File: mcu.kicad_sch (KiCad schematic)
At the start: 6 parts, among them U3 PCA9358

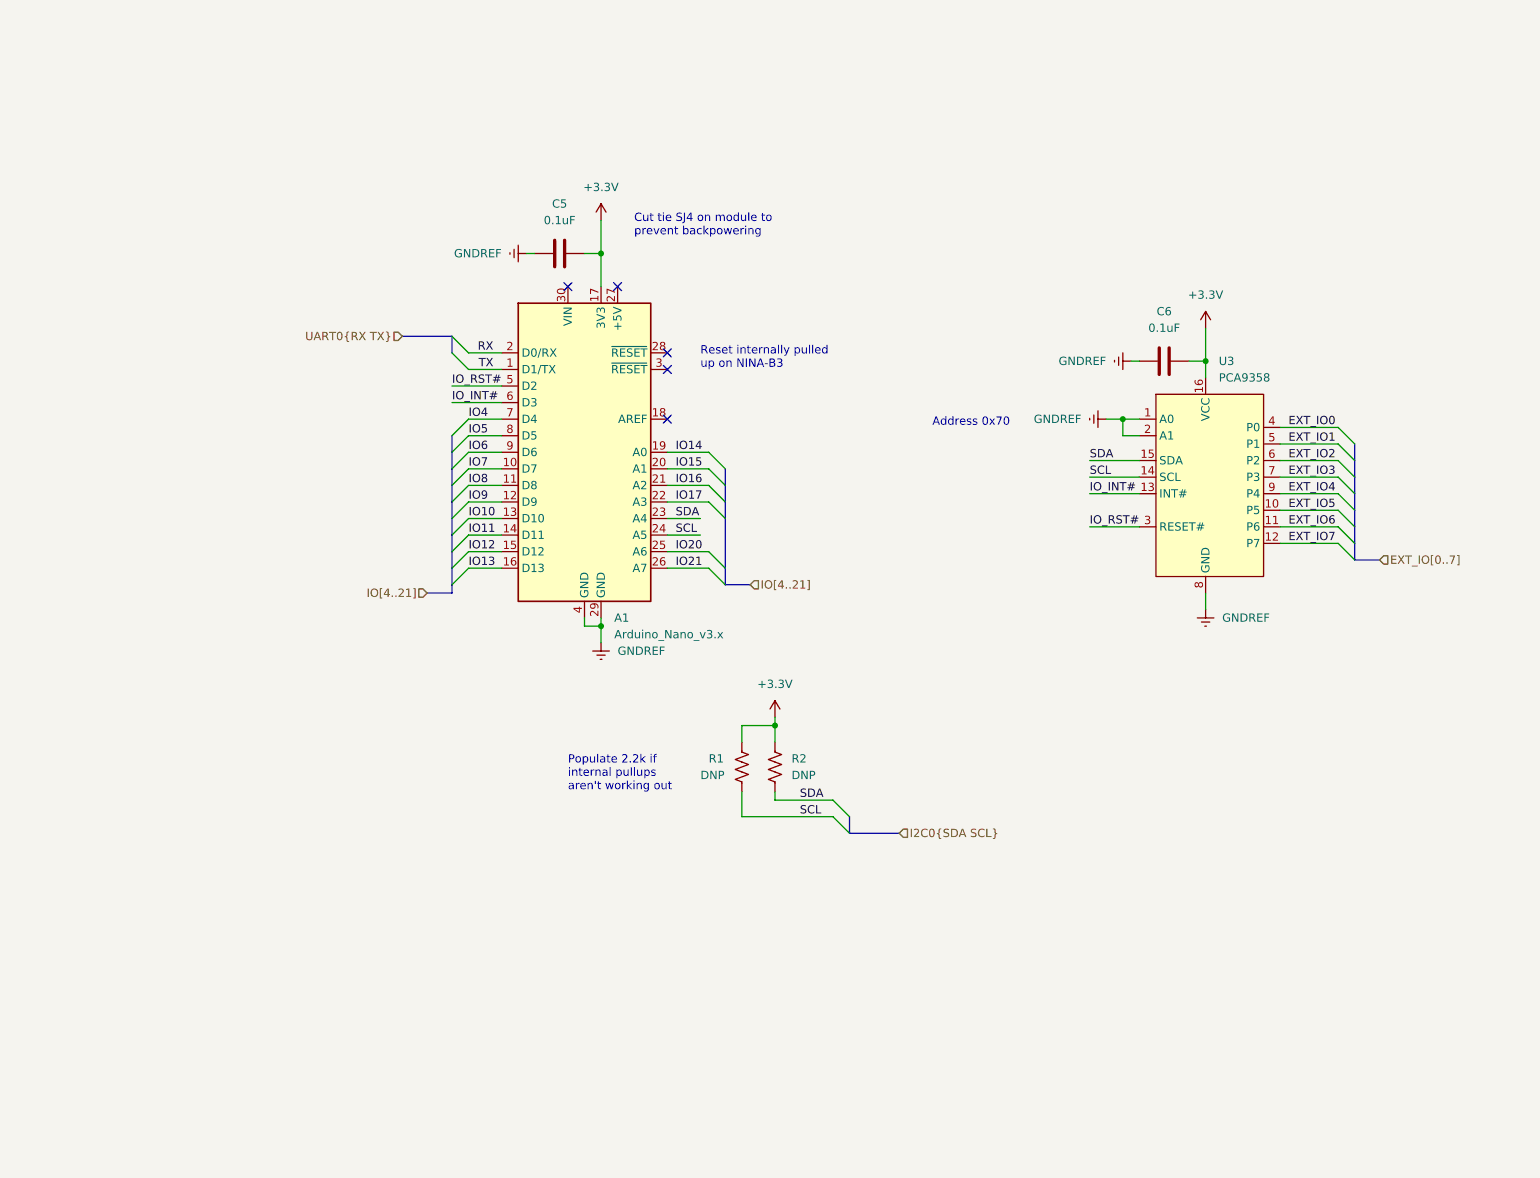
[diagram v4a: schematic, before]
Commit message: add compartment lights, switch to samd21j
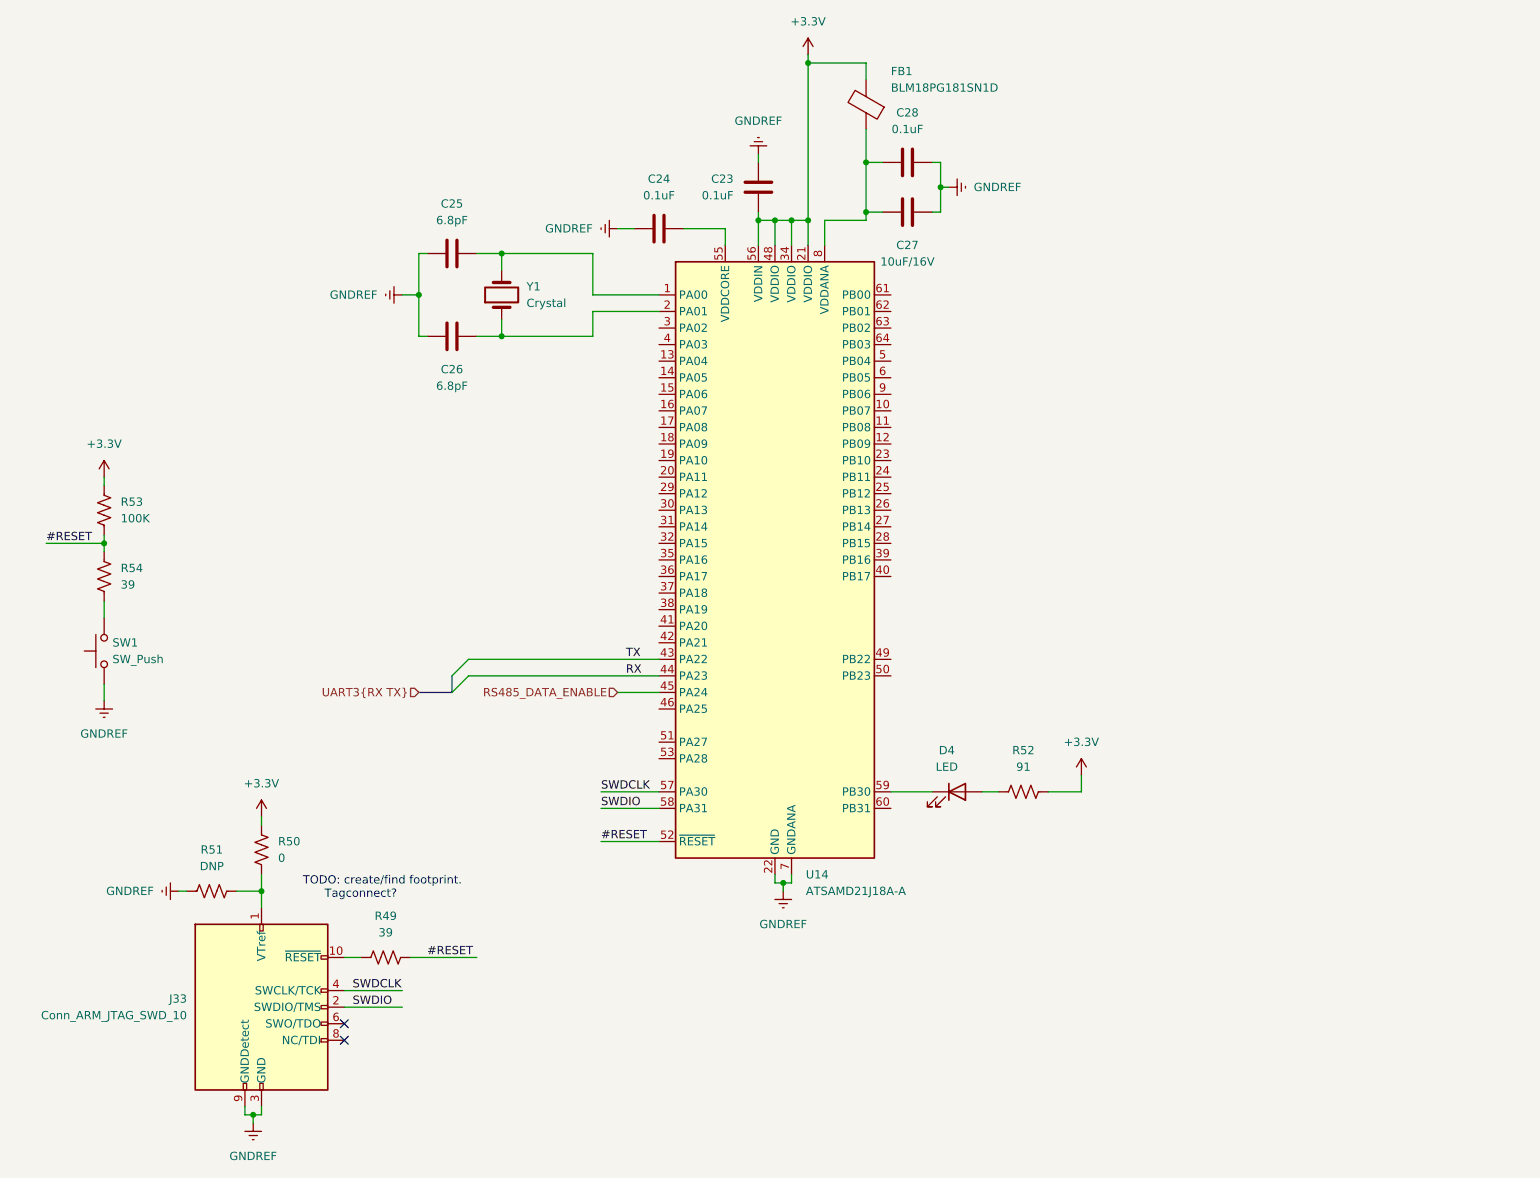
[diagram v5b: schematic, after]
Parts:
- removed A1: Arduino_Nano_v3.x, Module:Arduino_Nano, symbol MCU_Module:Arduino_Nano_v3.x
- removed C5, C6: 0.1uF, Capacitor_SMD:C_0805_2012Metric_Pad1.18x1.45mm_HandSolder, symbol Device:C
- removed R1, R2: DNP, Resistor_SMD:R_0805_2012Metric_Pad1.20x1.40mm_HandSolder, symbol Device:R_US
- removed U3: PCA9358, Package_SO:SOIC-16W_7.5x10.3mm_P1.27mm, symbol Toadly:PCA9358
- added C23, C24, C28: 0.1uF, Capacitor_SMD:C_0805_2012Metric_Pad1.18x1.45mm_HandSolder, symbol Device:C
- added C25, C26: 6.8pF, Capacitor_SMD:C_0805_2012Metric_Pad1.18x1.45mm_HandSolder, symbol Device:C
- added C27: 10uF/16V, Capacitor_SMD:C_0805_2012Metric_Pad1.18x1.45mm_HandSolder, symbol Device:C
- added D4: LED, LED_SMD:LED_0805_2012Metric_Pad1.15x1.40mm_HandSolder, symbol Device:LED
- added FB1: BLM18PG181SN1D, Inductor_SMD:L_0603_1608Metric_Pad1.05x0.95mm_HandSolder, symbol Device:FerriteBead
- added J33: Conn_ARM_JTAG_SWD_10, Connector_PinHeader_1.27mm:PinHeader_2x05_P1.27mm_Vertical_SMD, symbol Connector:Conn_ARM_JTAG_SWD_10
- added R49, R54: 39, Resistor_SMD:R_0805_2012Metric_Pad1.20x1.40mm_HandSolder, symbol Device:R_US
- added R50: 0, Resistor_SMD:R_0805_2012Metric_Pad1.20x1.40mm_HandSolder, symbol Device:R_US
- added R51: DNP, Resistor_SMD:R_0805_2012Metric_Pad1.20x1.40mm_HandSolder, symbol Device:R_US
- added R52: 91, Resistor_SMD:R_0805_2012Metric_Pad1.20x1.40mm_HandSolder, symbol Device:R_US
- added R53: 100K, Resistor_SMD:R_0805_2012Metric_Pad1.20x1.40mm_HandSolder, symbol Device:R_US
- added SW1: SW_Push, Button_Switch_SMD:SW_Push_1P1T_NO_6x6mm_H9.5mm, symbol Switch:SW_Push
- added U14: ATSAMD21J18A-A, Package_QFP:TQFP-64_10x10mm_P0.5mm, symbol MCU_Microchip_SAMD:ATSAMD21J18A-A
- added Y1: Crystal, symbol Device:Crystal
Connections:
- net +3.3V: now also C23.1, FB1.2, R50.2, R52.2, R53.2, U14.21 (VDDIO), U14.34 (VDDIO), U14.48 (VDDIO), U14.56 (VDDIN)
- net GNDREF: now also C23.2, C24.2, C25.1, C26.1, C27.1, C28.1, J33.3 (GND), J33.5 (GND), J33.9 (GNDDetect), R51.2, SW1.1, U14.22 (GND), U14.33 (GND), U14.47 (GND), U14.54 (GND), U14.7 (GNDANA)
- net RX: now also U14.44 (PA23)
- net TX: now also U14.43 (PA22)
- new net: J33.1 (VTref), R50.1, R51.1
- new net: J33.10 (~{RESET}), R49.1
- new net: C25.2, U14.1 (PA00), Y1.2
- new net: C26.2, U14.2 (PA01), Y1.1
- new net: C24.1, U14.55 (VDDCORE)
- new net: D4.1 (K), U14.59 (PB30)
- new net: C27.2, C28.2, FB1.1, U14.8 (VDDANA)
- new net: D4.2 (A), R52.1
- new net: R54.1, SW1.2
- new net #RESET: R49.2, R53.1, R54.2, U14.52 (~{RESET})
- new net RS485_DATA_ENABLE: U14.45 (PA24)
- new net SWDCLK: J33.4 (SWCLK/TCK), U14.57 (PA30)
- new net SWDIO: J33.2 (SWDIO/TMS), U14.58 (PA31)
- no-connect marks 5 -> 2
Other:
- note added: "TODO: create/find footprint. Tagconnect?"
- note removed: "Address 0x70"
- note removed: "Cut tie SJ4 on module to prevent backpowering"
- note removed: "Populate 2.2k if internal pullups aren't working out"
- note removed: "Reset internally pulled up on NINA-B3"

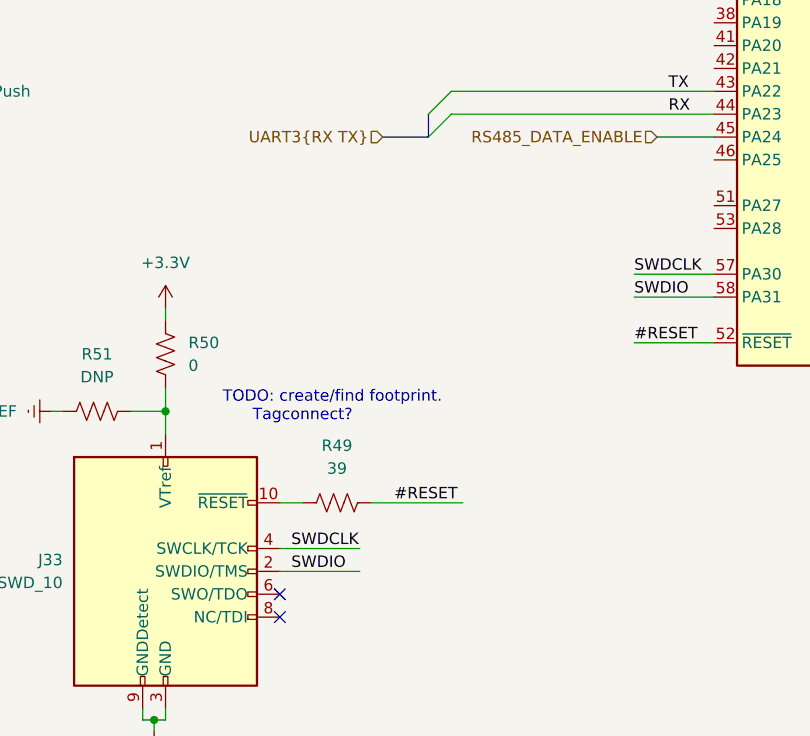
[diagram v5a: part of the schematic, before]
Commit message: remove drivers
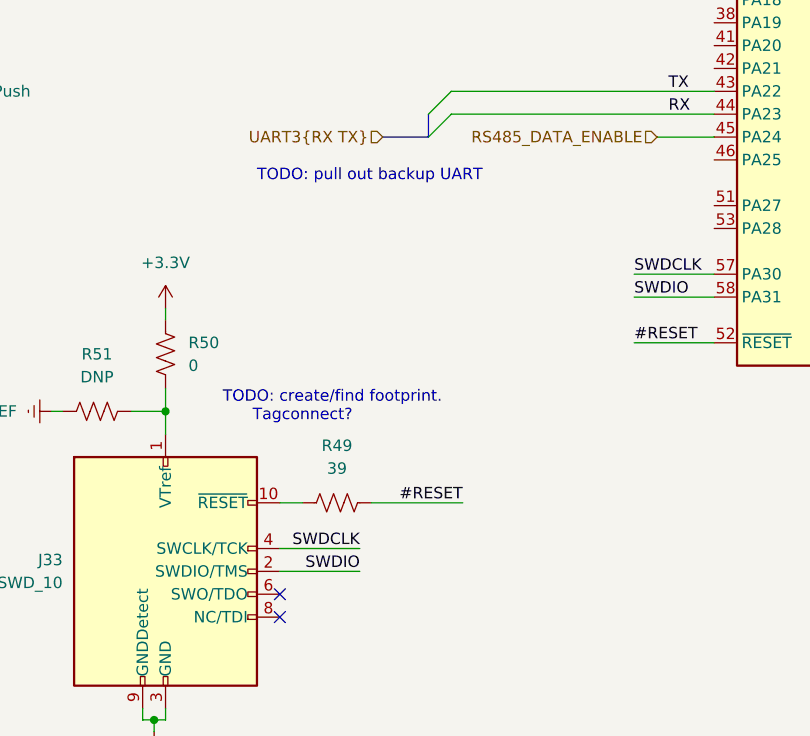
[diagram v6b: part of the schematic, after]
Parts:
- Y1: footprint (none) -> Crystal:Crystal_SMD_MicroCrystal_MS1V-T1K
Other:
- note added: "TODO: pull out backup UART"
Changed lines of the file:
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@@
     (stroke (width 0) (type default))
   )
+  (text "TODO: pull out backup UART" (at 63.5 121.92 0)
+    (effects (font (size 1.27 1.27)) (justify left bottom))
+  )
   (text "TODO: create/find footprint.\n      Tagconnect?" (at 59.69 148.59 0)
     (effects (font (size 1.27 1.27)) (justify left bottom))
@@
     (effects (font (size 1.27 1.27)) (justify left bottom))
   )
-  (label "#RESET" (at 78.74 157.48 0) (fields_autoplaced)
-    (effects (font (size 1.27 1.27)) (justify left bottom))
+  (label "#RESET" (at 86.36 157.48 180) (fields_autoplaced)
+    (effects (font (size 1.27 1.27)) (justify right bottom))
   )
   (label "TX" (at 109.22 111.76 0) (fields_autoplaced)
     (effects (font (size 1.27 1.27)) (justify left bottom))
   )
-  (label "SWDIO" (at 67.31 165.1 0) (fields_autoplaced)
-    (effects (font (size 1.27 1.27)) (justify left bottom))
-  )
-  (label "SWDCLK" (at 67.31 162.56 0) (fields_autoplaced)
-    (effects (font (size 1.27 1.27)) (justify left bottom))
+  (label "SWDIO" (at 74.93 165.1 180) (fields_autoplaced)
+    (effects (font (size 1.27 1.27)) (justify right bottom))
+  )
+  (label "SWDCLK" (at 74.93 162.56 180) (fields_autoplaced)
+    (effects (font (size 1.27 1.27)) (justify right bottom))
   )
   (label "SWDIO" (at 105.41 134.62 0) (fields_autoplaced)
@@
       (effects (font (size 1.27 1.27)) (justify right))
     )
-    (property "Footprint" "" (at 90.17 55.88 0)
-      (effects (font (size 1.27 1.27)) hide)
-    )
+    (property "Footprint" "Crystal:Crystal_SMD_MicroCrystal_MS1V-T1K" (at 90.17 55.88 0)
+      (effects (font (size 1.27 1.27)) hide)
+    )
